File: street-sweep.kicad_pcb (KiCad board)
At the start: 2 copper layers, 110.6 x 95.2 mm, 56 parts, among them J1 PJ-320A, P1 GT-USB-7010ASV, SW10 SW_Push, SW10_r1 SW_Push, SW11 SW_Push, SW11_r1 SW_Push, SW12 SW_Push, SW12_r1 SW_Push, SW13_r1 SW_Push, SW14 SW_Push, SW14_r1 SW_Push, SW15 SW_Push, SW15_r1 SW_Push, SW16 SW_Push, SW16_r1 SW_Push, SW17 SW_Push, SW17_r1 SW_Push, SW18 SW_Push, SW18_r1 SW_Push, SW2 SW_Push, SW20 SW_Push, SW21 SW_Push, SW2_r1 SW_Push, SW3 SW_Push, SW3_r1 SW_Push, SW4 SW_Push, SW4_r1 SW_Push, SW5 SW_Push, SW5_r1 SW_Push, SW6 SW_Push, SW6_r1 SW_Push, SW7_r1 SW_Push, SW8 SW_Push, SW8_r1 SW_Push, SW9 SW_Push, SW9_r1 SW_Push, U1 CH552G

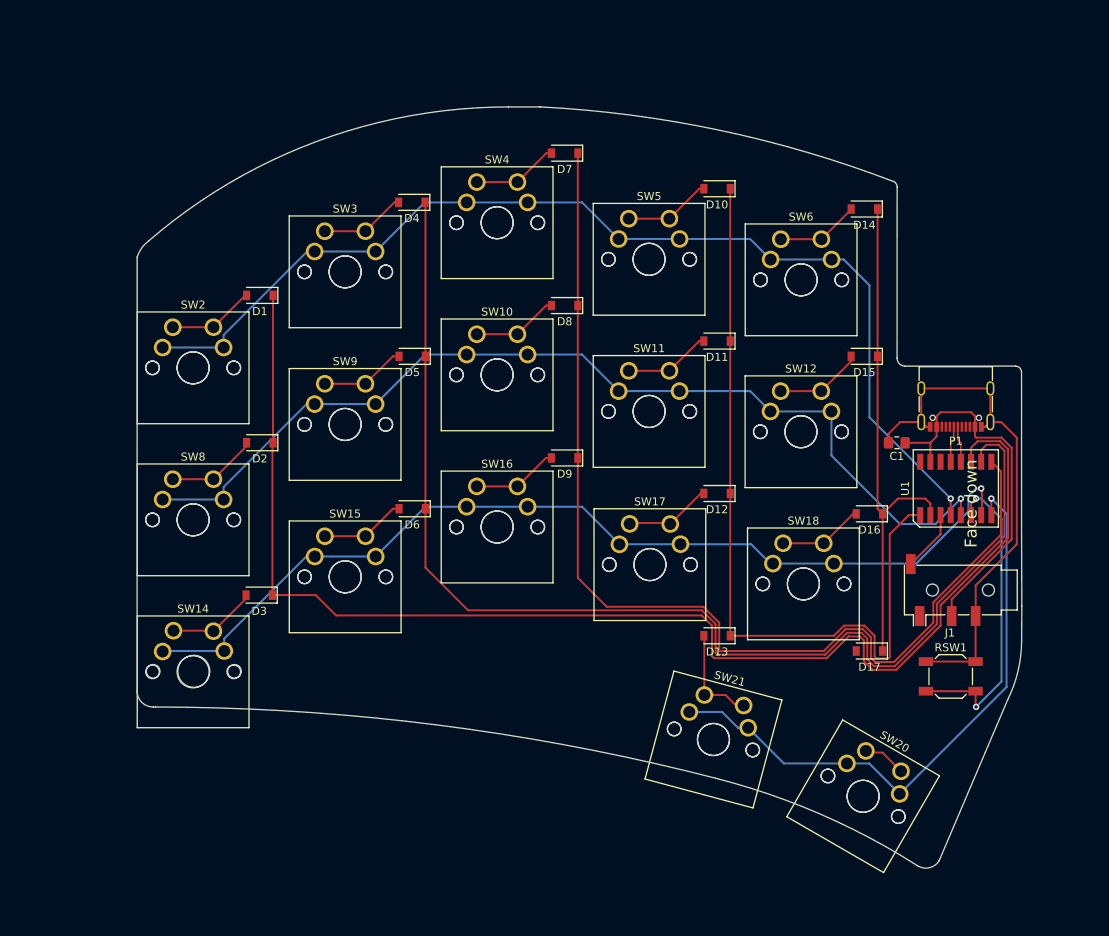
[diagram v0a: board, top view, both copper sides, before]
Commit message: Laid out CH552 Board version with two USB-C ports and fixes for flashing.
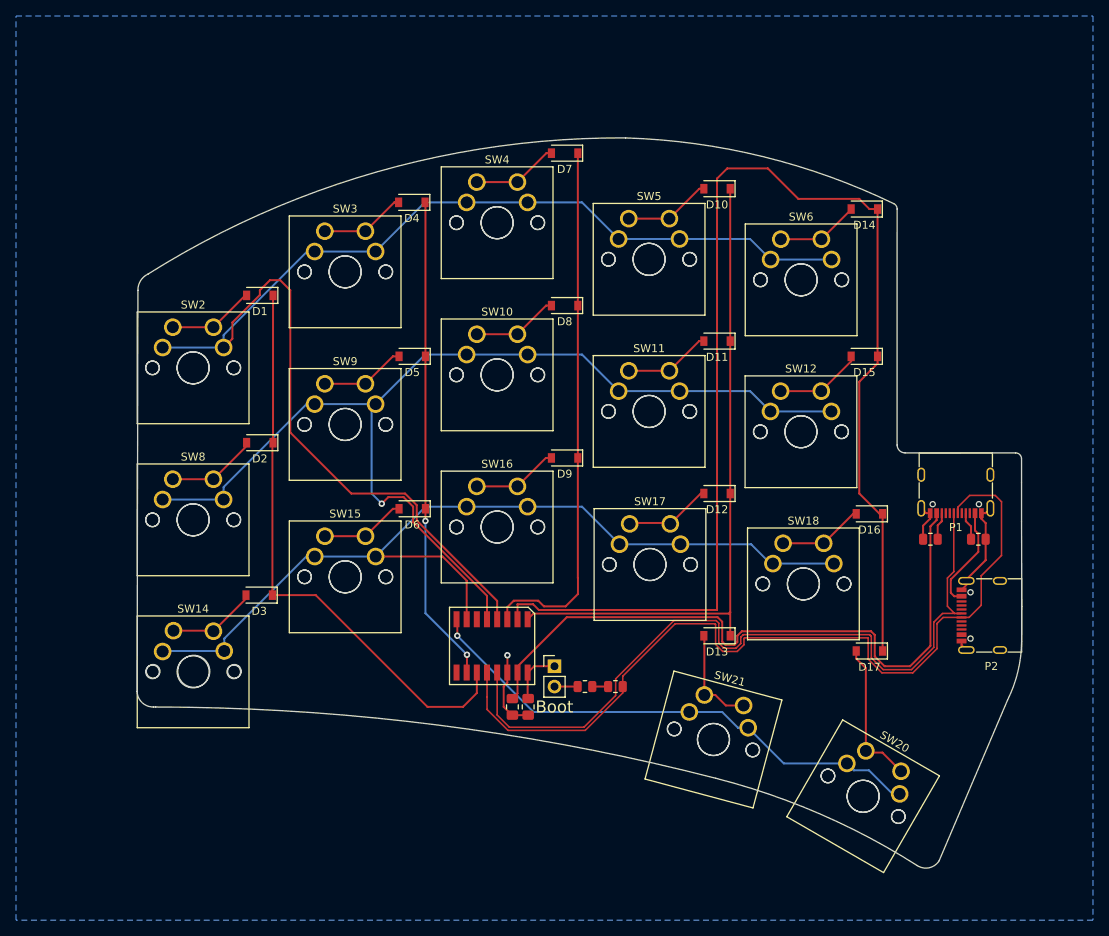
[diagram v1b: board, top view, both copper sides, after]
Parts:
- removed J1: PJ-320A, Connector_Audio:Jack_3.5mm_PJ320D_Horizontal
- removed RSW1: SKQGADE010, Button_Switch_SMD:SW_SPST_SKQG_WithoutStem
- added C2: 0.1uF, Capacitor_SMD:C_0805_2012Metric_Pad1.18x1.45mm_HandSolder, F.Cu at (84.3, 124.5)
- added JP1: Boot, Connector_PinHeader_2.54mm:PinHeader_1x02_P2.54mm_Vertical, F.Cu at (87.6, 119.4)
- added P2: GT-USB-7010ASV, Connector_USB:USB_C_Receptacle_G-Switch_GT-USB-7010ASV, F.Cu at (142.2, 113.0)
- added R1: 5.1k, Resistor_SMD:R_0805_2012Metric, F.Cu at (134.6, 103.5)
- added R2: 5.1k, Resistor_SMD:R_0805_2012Metric, F.Cu at (140.6, 103.5)
- added R3: 5.1k, Resistor_SMD:R_0805_2012Metric, F.Cu at (95.2, 121.9)
- added R4: 5.1k, Resistor_SMD:R_0805_2012Metric, F.Cu at (91.4, 121.9)
- moved U1 61.2 mm to (79.8, 116.8), turned to 180 degrees
- moved C1 58.3 mm to (82.4, 124.5), turned to -90 degrees
- moved P1 10.8 mm to (137.8, 96.5)
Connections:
- P1 pad A5: unconnected-(P1-PadA5) -> Net-(P1-PadA5)
- P1 pad B5: unconnected-(P1-PadB5) -> Net-(P1-PadB5)
- U1 pad 16: unconnected-(U1-Pad16) -> 3.3v
- U1 pad 3: Serial -> Column2
- U1 pad 6: reset -> unconnected-(U1-Pad6)
- U1 pad 9: Column2 -> unconnected-(U1-Pad9)
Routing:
- net D+: track 4.53 -> 108.1 mm
- net Column4: track 64.0 -> 161.4 mm
- net Column0: track 165.9 -> 72.1 mm
- net Column1: track 152.9 -> 61.0 mm, vias 0 -> 2
- net D-: track 4.53 -> 96.2 mm
- net Column2: track 133.9 -> 66.7 mm
- net vcc: track 47.0 -> 96.9 mm
- net reset: track 40.3 -> 0.00 mm, vias 2 -> 0
- net gnd: track 66.0 -> 29.1 mm, vias 0 -> 1
- net Row0: track 134.0 -> 164.7 mm, vias 1 -> 0
- net Column3: track 99.8 -> 81.6 mm
- net Switch16: track 5.45 -> 18.4 mm
- net Row3: track 75.8 -> 65.6 mm
- net Row2: track 121.8 -> 112.5 mm, vias 1 -> 0
- net Row1: track 123.6 -> 131.6 mm
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- added copper zone on B.Cu, net gnd
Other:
- board size 110.6 x 95.2 mm -> 110.6 x 91.3 mm
- board text added: "Boot"
- board text removed: "Face down"
- board text removed: "Face up"
